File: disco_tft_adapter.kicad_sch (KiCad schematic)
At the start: 21 parts, among them J1 QTH-030-02-L-D-A, J2 F31L-1A7H1-11030

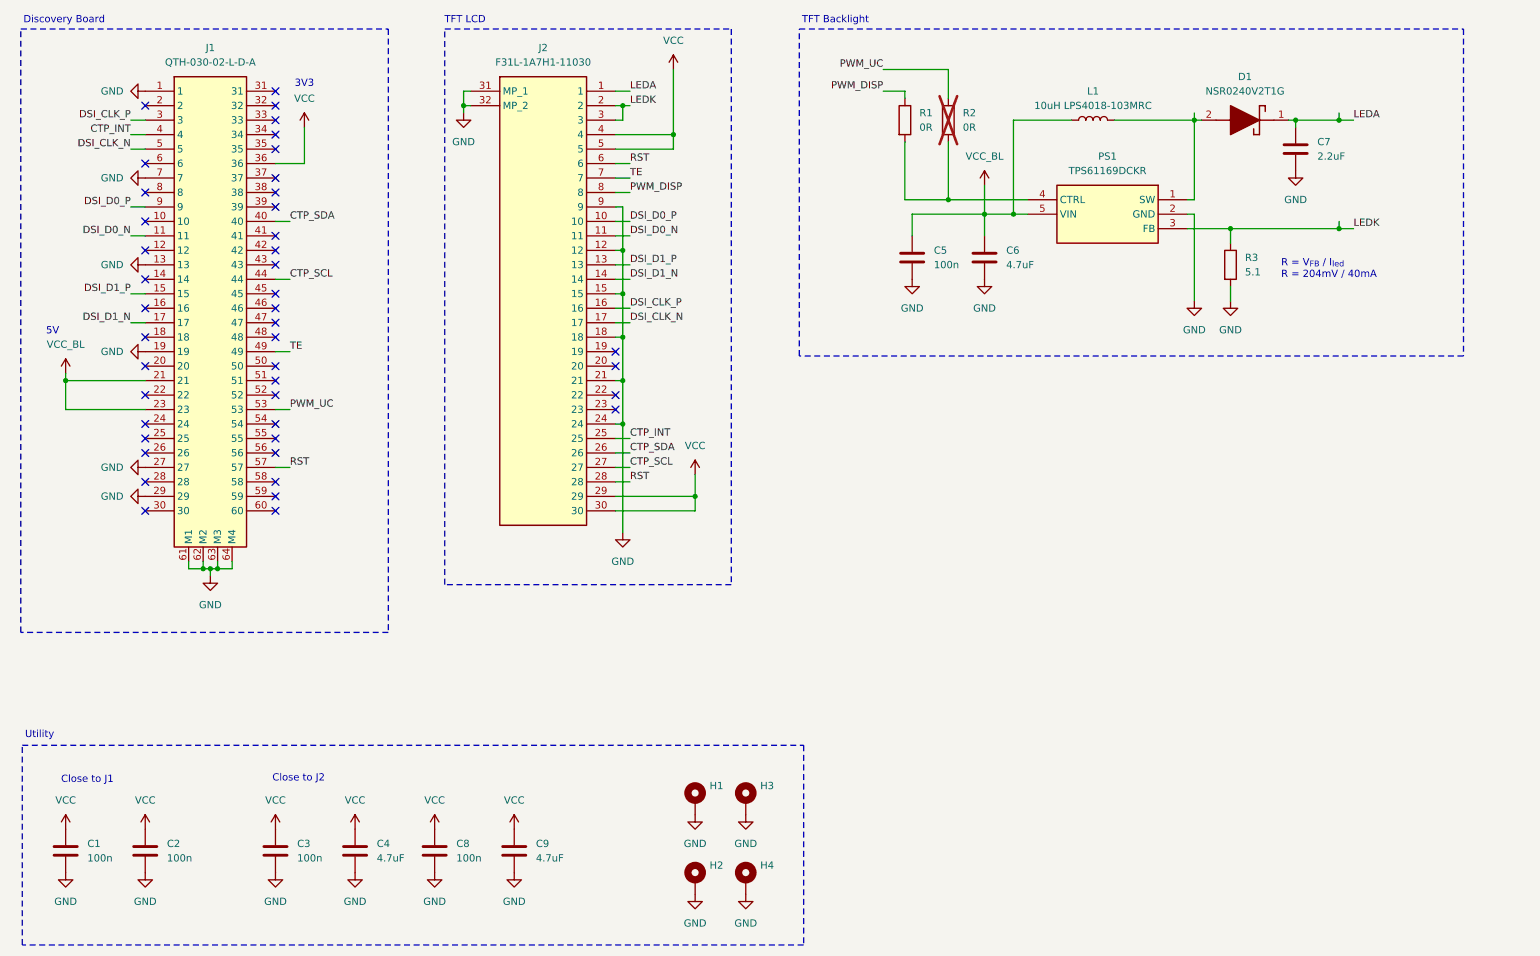
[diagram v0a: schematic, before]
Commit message: [schematics] update wiring acc to communication with display manufacturer
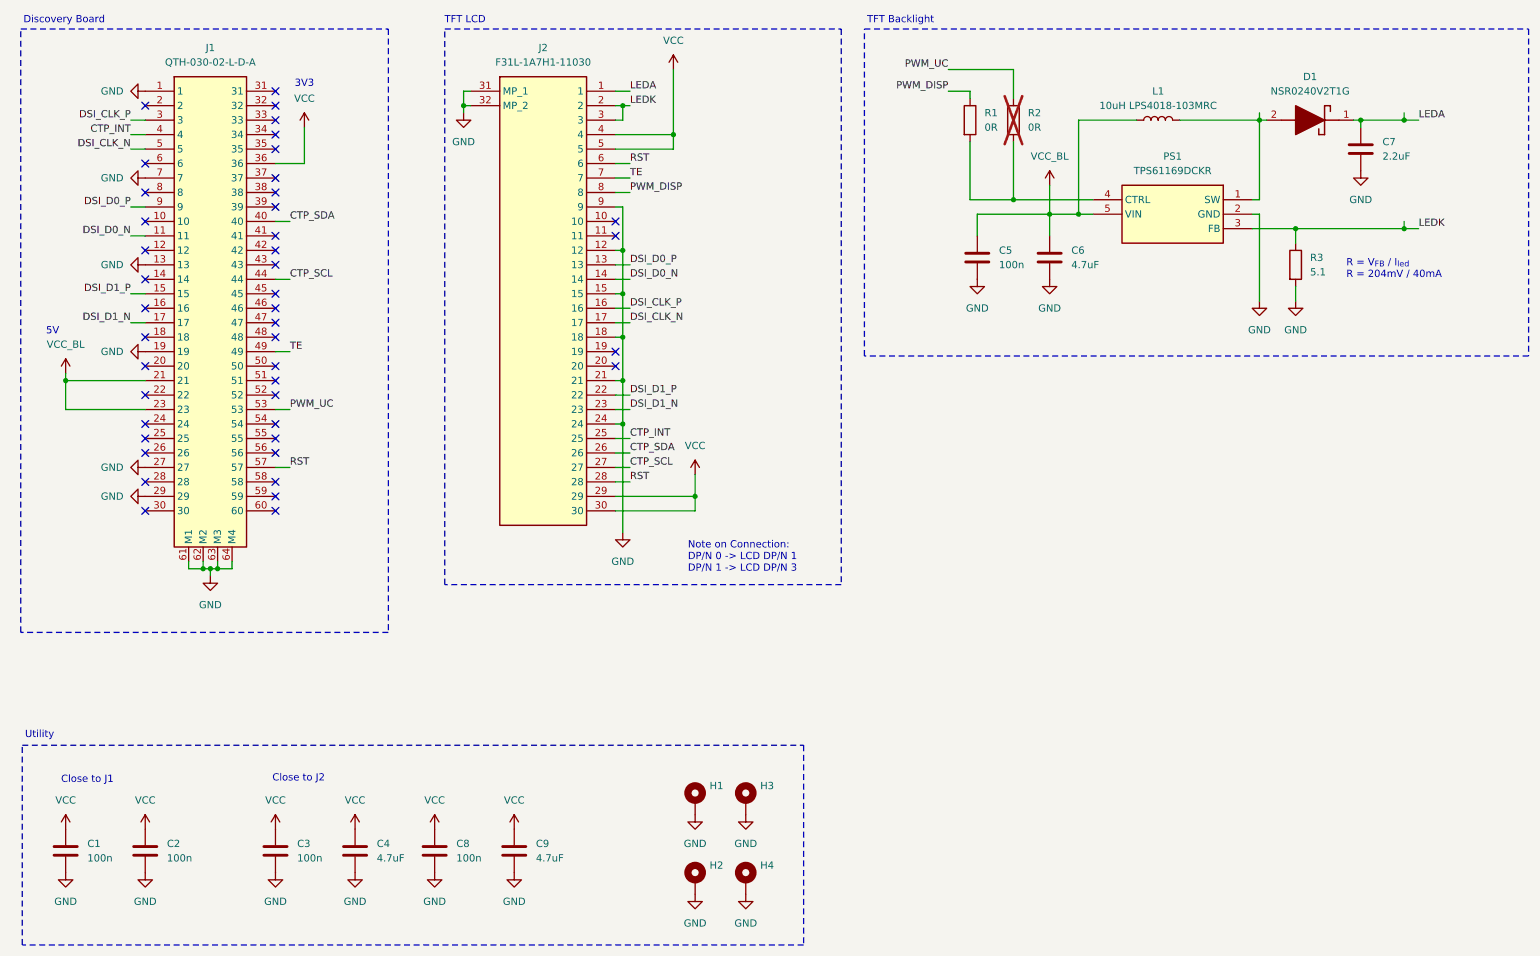
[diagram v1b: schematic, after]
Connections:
- net DSI_D0_N: now also J2.14; no longer J2.11
- net DSI_D0_P: now also J2.13; no longer J2.10
- net DSI_D1_N: now also J2.23; no longer J2.14
- net DSI_D1_P: now also J2.22; no longer J2.13
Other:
- note added: "Note on Connection: DP/N 0 -> LCD DP/N 1 DP/N 1 -> LCD DP/N 3"
- moved on the sheet: C5, C6, C7, D1, L1, PS1, R1, R2, R3

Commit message: [schematic] update footprints of small C and R to 0603
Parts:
- C1, C2, C3, C5, C8: footprint Capacitor_SMD:C_0201_0603Metric_Pad0.64x0.40mm_HandSolder -> Capacitor_SMD:C_0603_1608Metric
- R1, R2: footprint Resistor_SMD:R_0201_0603Metric_Pad0.64x0.40mm_HandSolder -> Resistor_SMD:R_0603_1608Metric
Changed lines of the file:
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@@
 			)
 		)
-		(property "Footprint" "Capacitor_SMD:C_0201_0603Metric_Pad0.64x0.40mm_HandSolder"
+		(property "Footprint" "Capacitor_SMD:C_0603_1608Metric"
 			(at 40.3352 166.37 0)
 			(hide yes)
@@
 			)
 		)
-		(property "Footprint" "Capacitor_SMD:C_0201_0603Metric_Pad0.64x0.40mm_HandSolder"
+		(property "Footprint" "Capacitor_SMD:C_0603_1608Metric"
 			(at 26.3652 166.37 0)
 			(hide yes)
@@
 			)
 		)
-		(property "Footprint" "Resistor_SMD:R_0201_0603Metric_Pad0.64x0.40mm_HandSolder"
+		(property "Footprint" "Resistor_SMD:R_0603_1608Metric"
 			(at 182.372 34.29 90)
 			(hide yes)
@@
 			)
 		)
-		(property "Footprint" "Capacitor_SMD:C_0201_0603Metric_Pad0.64x0.40mm_HandSolder"
+		(property "Footprint" "Capacitor_SMD:C_0603_1608Metric"
 			(at 186.3852 62.23 0)
 			(hide yes)
@@
 			)
 		)
-		(property "Footprint" "Resistor_SMD:R_0201_0603Metric_Pad0.64x0.40mm_HandSolder"
+		(property "Footprint" "Resistor_SMD:R_0603_1608Metric"
 			(at 189.992 34.29 90)
 			(hide yes)
@@
 			)
 		)
-		(property "Footprint" "Capacitor_SMD:C_0201_0603Metric_Pad0.64x0.40mm_HandSolder"
+		(property "Footprint" "Capacitor_SMD:C_0603_1608Metric"
 			(at 91.1352 166.37 0)
 			(hide yes)
@@
 			)
 		)
-		(property "Footprint" "Capacitor_SMD:C_0201_0603Metric_Pad0.64x0.40mm_HandSolder"
+		(property "Footprint" "Capacitor_SMD:C_0603_1608Metric"
 			(at 63.1952 166.37 0)
 			(hide yes)

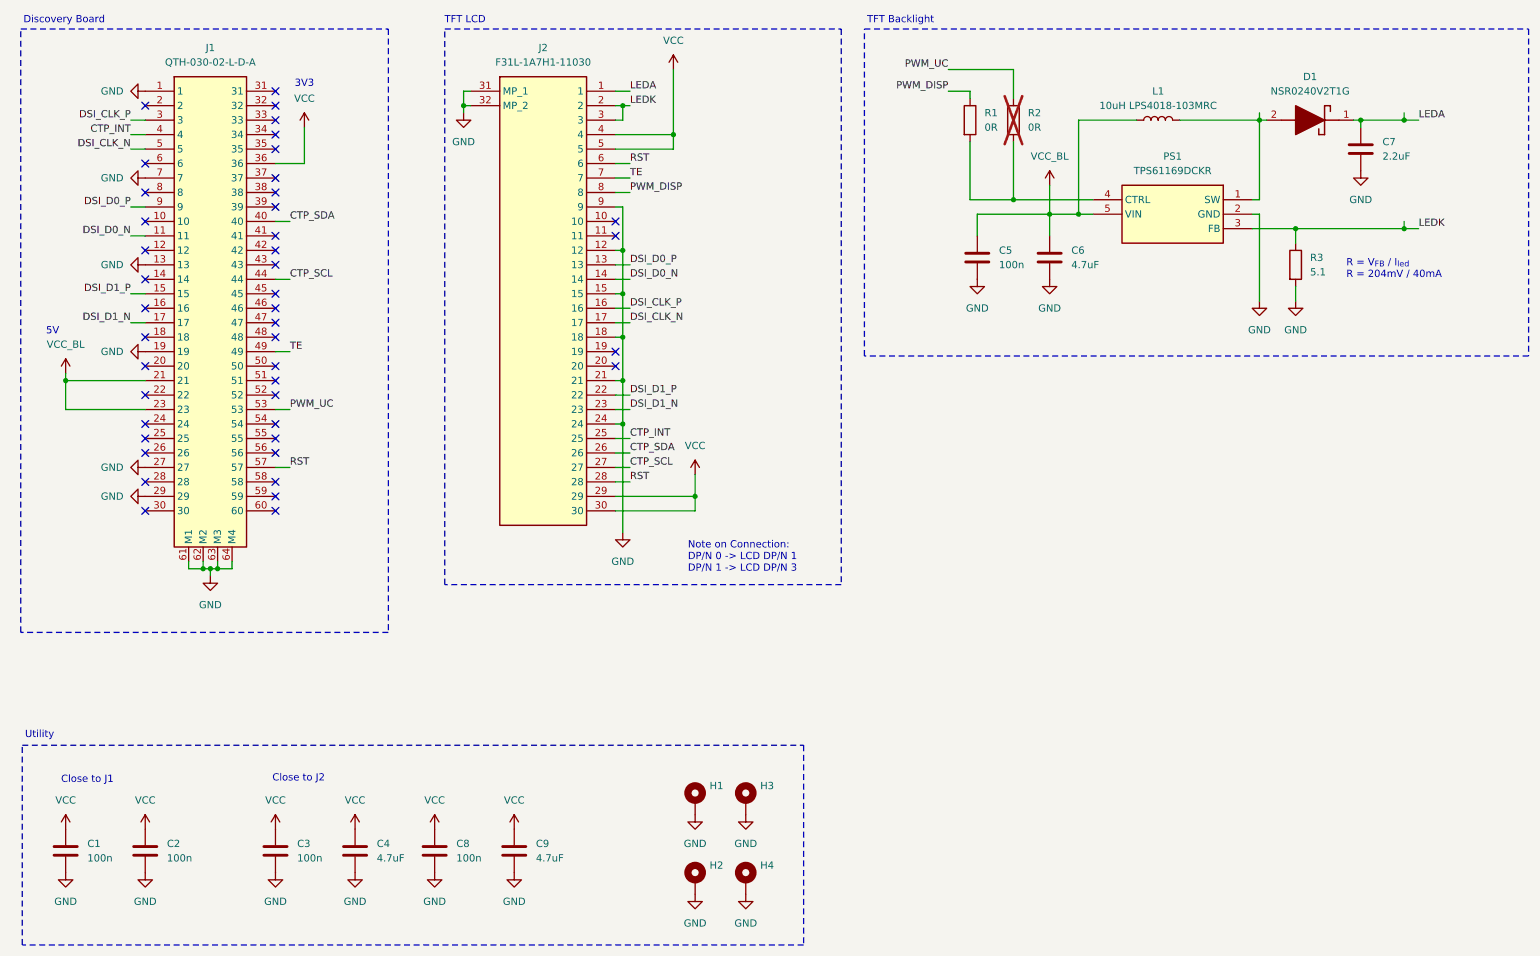
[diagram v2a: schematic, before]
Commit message: [all] add test points using a custom footprint
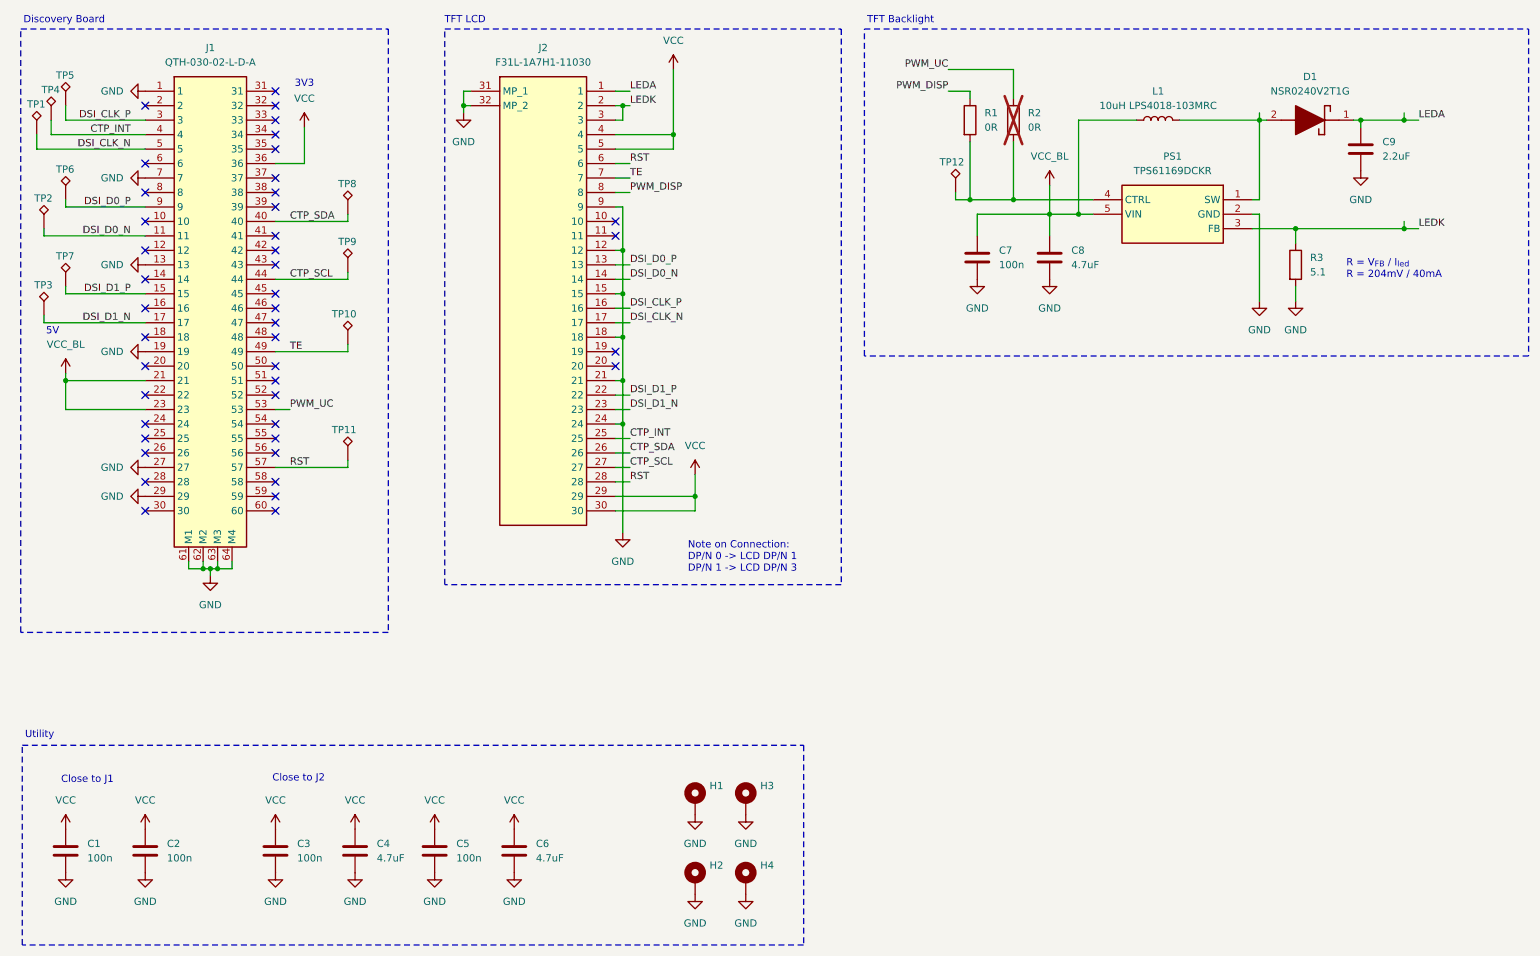
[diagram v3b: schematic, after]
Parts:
- added TP1, TP10, TP11, TP12, TP2, TP3, TP4, TP5, TP6, TP7, TP8, TP9: TestPoint_Alt, aa_prj:TestPoint_TP_D0.5mm, symbol Connector:TestPoint_Alt
- renumbered C8 to C5, C9 to C6, C5 to C7, C6 to C8, C7 to C9
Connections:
- net CTP_INT: now also TP4.1
- net CTP_SCL: now also TP9.1
- net CTP_SDA: now also TP8.1
- net DSI_CLK_N: now also TP1.1
- net DSI_CLK_P: now also TP5.1
- net DSI_D0_N: now also TP2.1
- net DSI_D0_P: now also TP6.1
- net DSI_D1_N: now also TP3.1
- net DSI_D1_P: now also TP7.1
- net RST: now also TP11.1
- net TE: now also TP10.1
- net at PS1.4 (CTRL), R1.2, R2.2: now also TP12.1
